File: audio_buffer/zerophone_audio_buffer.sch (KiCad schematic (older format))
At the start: 7 parts, among them P1 INPUT_CONN, P2 OUTPUT_CONN, U1 LM1117-2.5, U2 NC7WZ16

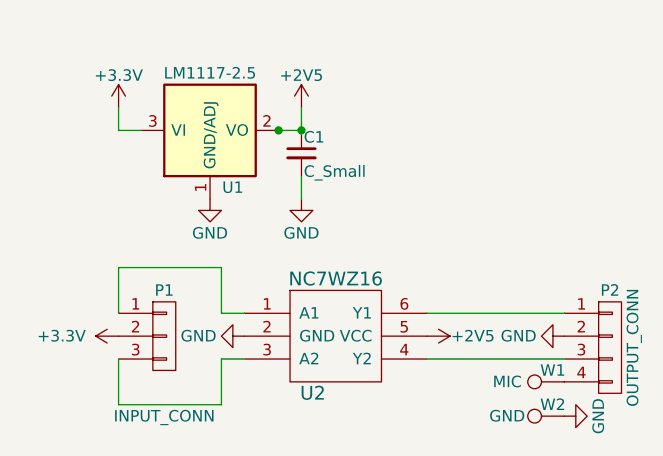
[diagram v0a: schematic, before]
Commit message: Updated audio buffer board
-Changed power regulator to a low-noise one
-Moved GND testpoint so that adding a connector is  theoretically
possible, just in case
-Added auxiliary axis
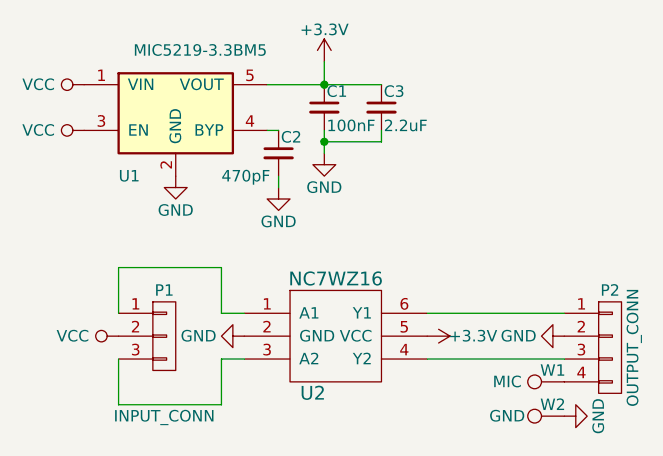
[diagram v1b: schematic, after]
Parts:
- removed U1: LM1117-2.5, TO_SOT_Packages_SMD:SOT-223, symbol LM1117-2.5
- added C2: 470pF, Capacitors_SMD:C_0603_HandSoldering, symbol C_Small
- added C3: 2.2uF, Capacitors_SMD:C_0603_HandSoldering, symbol C_Small
- added U1: MIC5219-3.3BM5, TO_SOT_Packages_SMD:SOT-23-5, symbol MIC5219-3.3BM5
- C1: value C_Small -> 100nF; footprint Capacitors_SMD:C_0805_HandSoldering -> Capacitors_SMD:C_0603_HandSoldering
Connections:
- net +2V5 is gone; now on net +3V3: C1.1, U2.5 (VCC)
- net +3V3: now also C3.1, U1.5 (VOUT); no longer P1.2 (P2)
- net GND: now also C2.2, C3.2, U1.2 (GND)
- new net: C2.1, U1.4 (BYP)
- new net VCC: P1.2 (P2), U1.1 (VIN), U1.3 (EN)
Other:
- moved on the sheet: C1
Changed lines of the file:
@@
 	0    1    1    0
 $EndComp
-$Comp
-L LM1117-2.5 U1
-U 1 1 58BC819D
-P 3300 1700
-F 0 "U1" H 3400 1450 50  0000 C CNN
-F 1 "LM1117-2.5" H 3300 1950 50  0000 C CNN
-F 2 "TO_SOT_Packages_SMD:SOT-223" H 3300 1700 50  0001 C CNN
-F 3 "" H 3300 1700 50  0000 C CNN
-	1    3300 1700
-	1    0    0    -1
-$EndComp
-Wire Wire Line
-	2900 1600 2900 1700
-Wire Wire Line
-	2900 1700 3000 1700
-Wire Wire Line
-	3700 1600 3700 1700
-Wire Wire Line
-	3700 1700 3600 1700
+Wire Wire Line
+	3800 1500 3800 1400
+Wire Wire Line
+	3550 1500 4050 1500
 $Comp
 L GND #PWR03
 U 1 1 58BC8213
-P 3300 2000
-F 0 "#PWR03" H 3300 1750 50  0001 C CNN
-F 1 "GND" H 3300 1850 50  0000 C CNN
-F 2 "" H 3300 2000 50  0000 C CNN
-F 3 "" H 3300 2000 50  0000 C CNN
-	1    3300 2000
+P 3150 1900
+F 0 "#PWR03" H 3150 1650 50  0001 C CNN
+F 1 "GND" H 3150 1750 50  0000 C CNN
+F 2 "" H 3150 1900 50  0000 C CNN
+F 3 "" H 3150 1900 50  0000 C CNN
+	1    3150 1900
 	1    0    0    -1
 $EndComp
@@
 L C_Small C1
 U 1 1 58BC827C
-P 3700 1800
-F 0 "C1" H 3710 1870 50  0000 L CNN
-F 1 "C_Small" H 3710 1720 50  0000 L CNN
-F 2 "Capacitors_SMD:C_0805_HandSoldering" H 3700 1800 50  0001 C CNN
-F 3 "" H 3700 1800 50  0000 C CNN
-	1    3700 1800
-	1    0    0    -1
-$EndComp
-Wire Wire Line
-	3700 2000 3700 1900
+P 3800 1600
+F 0 "C1" H 3810 1670 50  0000 L CNN
+F 1 "100nF" H 3810 1520 50  0000 L CNN
+F 2 "Capacitors_SMD:C_0603_HandSoldering" H 3800 1600 50  0001 C CNN
+F 3 "" H 3800 1600 50  0000 C CNN
+	1    3800 1600
+	1    0    0    -1
+$EndComp
+Wire Wire Line
+	3800 1800 3800 1700
 $Comp
 L GND #PWR04
 U 1 1 58BC84D9
-P 3700 2000
-F 0 "#PWR04" H 3700 1750 50  0001 C CNN
-F 1 "GND" H 3700 1850 50  0000 C CNN
-F 2 "" H 3700 2000 50  0000 C CNN
-F 3 "" H 3700 2000 50  0000 C CNN
-	1    3700 2000
+P 3800 1800
+F 0 "#PWR04" H 3800 1550 50  0001 C CNN
+F 1 "GND" H 3800 1650 50  0000 C CNN
+F 2 "" H 3800 1800 50  0000 C CNN
+F 3 "" H 3800 1800 50  0000 C CNN
+	1    3800 1800
 	1    0    0    -1
 $EndComp
@@
 	0    -1   -1   0
 $EndComp
-Connection ~ 3600 1700
-Connection ~ 3700 1700
+Connection ~ 3800 1500
 Wire Wire Line
 	2900 2500 2900 2300
@@
 L +3.3V #PWR06
 U 1 1 58C39217
-P 2900 1600
-F 0 "#PWR06" H 2900 1450 50  0001 C CNN
-F 1 "+3.3V" H 2900 1740 50  0000 C CNN
-F 2 "" H 2900 1600 50  0000 C CNN
-F 3 "" H 2900 1600 50  0000 C CNN
-	1    2900 1600
+P 3800 1400
+F 0 "#PWR06" H 3800 1250 50  0001 C CNN
+F 1 "+3.3V" H 3800 1540 50  0000 C CNN
+F 2 "" H 3800 1400 50  0000 C CNN
+F 3 "" H 3800 1400 50  0000 C CNN
+	1    3800 1400
+	1    0    0    -1
+$EndComp
+$Comp
+L MIC5219-3.3BM5 U1
+U 1 1 59A81EE9
+P 3150 1600
+F 0 "U1" H 2900 1300 50  0000 L CNN
+F 1 "MIC5219-3.3BM5" H 3550 1850 50  0000 R CNN
+F 2 "TO_SOT_Packages_SMD:SOT-23-5" H 3800 1350 50  0001 C CIN
+F 3 "" H 3150 1600 50  0000 C CNN
+	1    3150 1600
 	1    0    0    -1
 $EndComp
 $Comp
 L +3.3V #PWR07
-U 1 1 58C3929D
-P 2900 2600
-F 0 "#PWR07" H 2900 2450 50  0001 C CNN
-F 1 "+3.3V" V 2900 2850 50  0000 C CNN
-F 2 "" H 2900 2600 50  0000 C CNN
-F 3 "" H 2900 2600 50  0000 C CNN
-	1    2900 2600
-	0    -1   -1   0
-$EndComp
-$Comp
-L +2V5 #PWR08
-U 1 1 58C392E1
-P 3700 1600
-F 0 "#PWR08" H 3700 1450 50  0001 C CNN
-F 1 "+2V5" H 3700 1740 50  0000 C CNN
-F 2 "" H 3700 1600 50  0000 C CNN
-F 3 "" H 3700 1600 50  0000 C CNN
-	1    3700 1600
-	1    0    0    -1
-$EndComp
-$Comp
-L +2V5 #PWR09
-U 1 1 58C3934E
+U 1 1 59A81FF3
 P 4250 2600
-F 0 "#PWR09" H 4250 2450 50  0001 C CNN
-F 1 "+2V5" V 4250 2800 50  0000 C CNN
+F 0 "#PWR07" H 4250 2450 50  0001 C CNN
+F 1 "+3.3V" V 4250 2800 50  0000 C CNN
 F 2 "" H 4250 2600 50  0000 C CNN
 F 3 "" H 4250 2600 50  0000 C CNN
@@
 	0    1    1    0
 $EndComp
+$Comp
+L VCC #PWR08
+U 1 1 59A820B9
+P 2750 1700
+F 0 "#PWR08" H 2750 1550 50  0001 C CNN
+F 1 "VCC" V 2750 1900 50  0000 C CNN
+F 2 "" H 2750 1700 50  0001 C CNN
+F 3 "" H 2750 1700 50  0001 C CNN
+	1    2750 1700
+	0    -1   -1   0
+$EndComp
+$Comp
+L VCC #PWR09
+U 1 1 59A8210A
+P 2750 1500
+F 0 "#PWR09" H 2750 1350 50  0001 C CNN
+F 1 "VCC" V 2750 1700 50  0000 C CNN
+F 2 "" H 2750 1500 50  0001 C CNN
+F 3 "" H 2750 1500 50  0001 C CNN
+	1    2750 1500
+	0    -1   -1   0
+$EndComp
+$Comp
+L VCC #PWR010
+U 1 1 59A8212A
+P 2900 2600
+F 0 "#PWR010" H 2900 2450 50  0001 C CNN
+F 1 "VCC" V 2900 2800 50  0000 C CNN
+F 2 "" H 2900 2600 50  0001 C CNN
+F 3 "" H 2900 2600 50  0001 C CNN
+	1    2900 2600
+	0    -1   -1   0
+$EndComp
+$Comp
+L C_Small C2
+U 1 1 59A821C6
+P 3600 1800
+F 0 "C2" H 3610 1870 50  0000 L CNN
+F 1 "470pF" H 3350 1700 50  0000 L CNN
+F 2 "Capacitors_SMD:C_0603_HandSoldering" H 3600 1800 50  0001 C CNN
+F 3 "" H 3600 1800 50  0001 C CNN
+	1    3600 1800
+	1    0    0    -1
+$EndComp
+$Comp
+L GND #PWR011
+U 1 1 59A82248
+P 3600 1950
+F 0 "#PWR011" H 3600 1700 50  0001 C CNN
+F 1 "GND" H 3600 1800 50  0000 C CNN
+F 2 "" H 3600 1950 50  0000 C CNN
+F 3 "" H 3600 1950 50  0000 C CNN
+	1    3600 1950
+	1    0    0    -1
+$EndComp
+Wire Wire Line
+	3550 1700 3600 1700
+Wire Wire Line
+	3600 1900 3600 1950
+$Comp
+L C_Small C3
+U 1 1 59A8233C
+P 4050 1600
+F 0 "C3" H 4060 1670 50  0000 L CNN
+F 1 "2.2uF" H 4060 1520 50  0000 L CNN
+F 2 "Capacitors_SMD:C_0603_HandSoldering" H 4050 1600 50  0001 C CNN
+F 3 "" H 4050 1600 50  0000 C CNN
+	1    4050 1600
+	1    0    0    -1
+$EndComp
+Wire Wire Line
+	3800 1750 4050 1750
+Wire Wire Line
+	4050 1750 4050 1700
+Connection ~ 3800 1750
 $EndSCHEMATC
